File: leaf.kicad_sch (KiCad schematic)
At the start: 0 parts

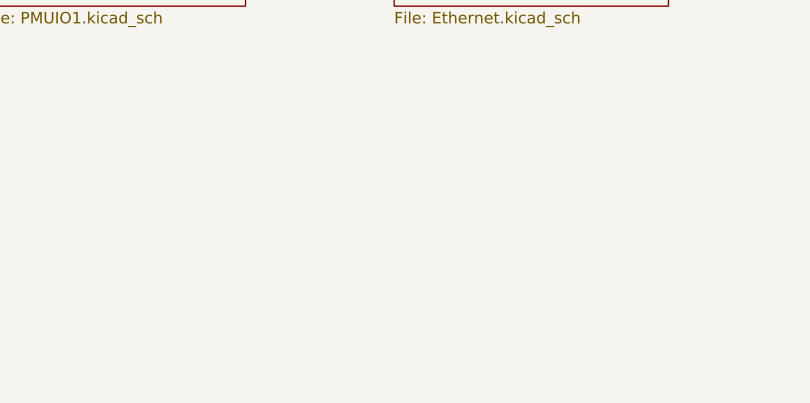
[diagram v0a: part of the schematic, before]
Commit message: placed RK809 components
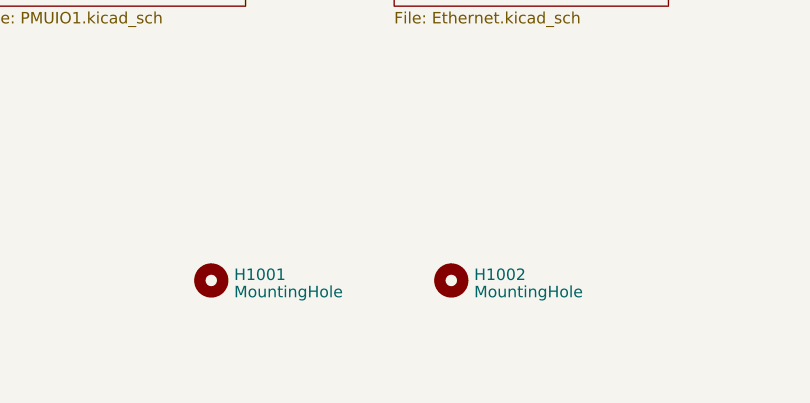
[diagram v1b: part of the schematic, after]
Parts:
- added H1001, H1002: MountingHole, MountingHole:MountingHole_2.7mm_M2.5, symbol Mechanical:MountingHole
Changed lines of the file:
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@@
     (effects (font (size 1.27 1.27)) (justify right bottom))
+  )
+  (symbol (lib_id "Mechanical:MountingHole") (at 106.68 144.78 0) (unit 1)
+    (in_bom yes) (on_board yes) (dnp no) (fields_autoplaced)
+    (property "Reference" "H1001" (at 109.22 144.1363 0)
+      (effects (font (size 1.27 1.27)) (justify left))
+    )
+    (property "Value" "MountingHole" (at 109.22 146.0573 0)
+      (effects (font (size 1.27 1.27)) (justify left))
+    )
+    (property "Footprint" "MountingHole:MountingHole_2.7mm_M2.5" (at 106.68 144.78 0)
+      (effects (font (size 1.27 1.27)) hide)
+    )
+    (property "Datasheet" "~" (at 106.68 144.78 0)
+      (effects (font (size 1.27 1.27)) hide)
+    )
+    (instances
+      (project "leaf"
+        (path "/e3b58043-16a3-43c8-9fad-9c9784eebfa4"
+          (reference "H1001") (unit 1)
+        )
+      )
+    )
+  )
+  (symbol (lib_id "Mechanical:MountingHole") (at 133.35 144.78 0) (unit 1)
+    (in_bom yes) (on_board yes) (dnp no) (fields_autoplaced)
+    (property "Reference" "H1002" (at 135.89 144.1363 0)
+      (effects (font (size 1.27 1.27)) (justify left))
+    )
+    (property "Value" "MountingHole" (at 135.89 146.0573 0)
+      (effects (font (size 1.27 1.27)) (justify left))
+    )
+    (property "Footprint" "MountingHole:MountingHole_2.7mm_M2.5" (at 133.35 144.78 0)
+      (effects (font (size 1.27 1.27)) hide)
+    )
+    (property "Datasheet" "~" (at 133.35 144.78 0)
+      (effects (font (size 1.27 1.27)) hide)
+    )
+    (instances
+      (project "leaf"
+        (path "/e3b58043-16a3-43c8-9fad-9c9784eebfa4"
+          (reference "H1002") (unit 1)
+        )
+      )
+    )
   )
   (sheet (at 81.28 69.85) (size 29.21 17.78) (fields_autoplaced)

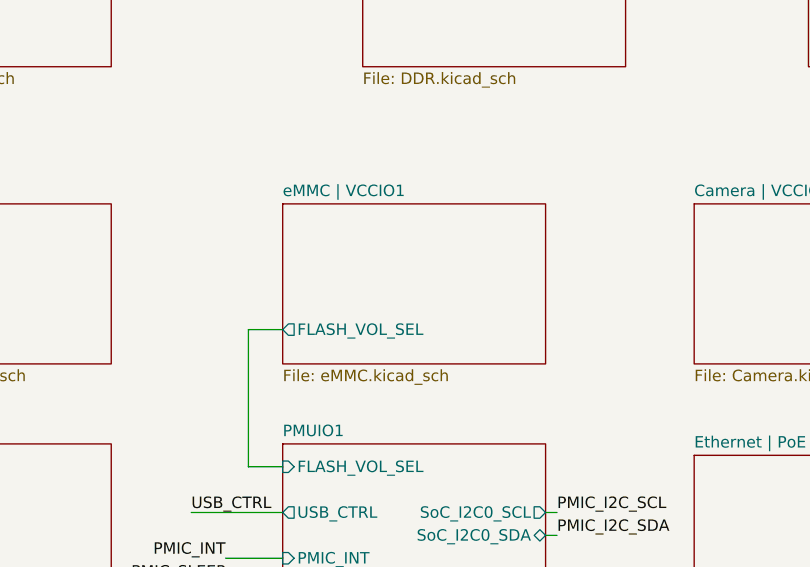
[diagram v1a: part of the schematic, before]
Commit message: rename emmc to vccio1
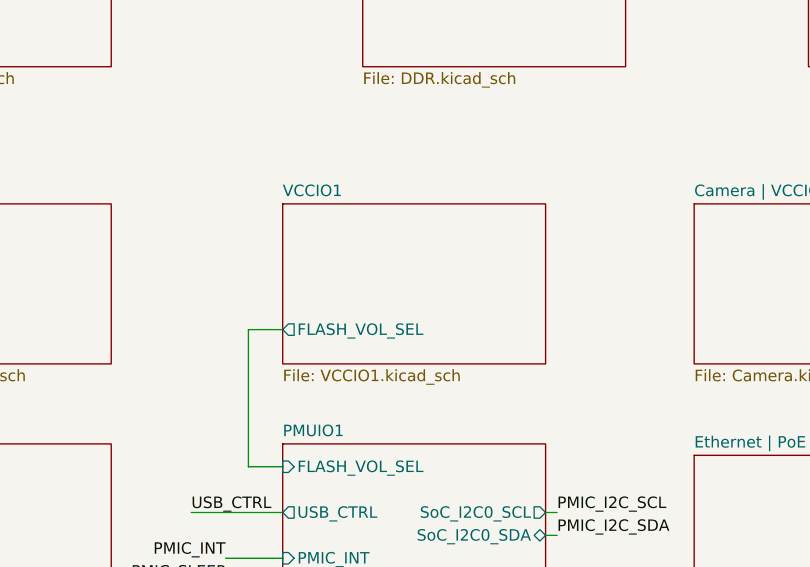
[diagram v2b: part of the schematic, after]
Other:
- sheet eMMC | VCCIO1 renamed VCCIO1
- sheet VCCIO1: file eMMC.kicad_sch -> VCCIO1.kicad_sch
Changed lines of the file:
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@@
     (stroke (width 0.1524) (type solid))
     (fill (color 0 0 0 0.0000))
-    (property "Sheetname" "eMMC | VCCIO1" (at 81.28 69.1384 0)
+    (property "Sheetname" "VCCIO1" (at 81.28 69.1384 0)
       (effects (font (size 1.27 1.27)) (justify left bottom))
     )
-    (property "Sheetfile" "eMMC.kicad_sch" (at 81.28 88.2146 0)
+    (property "Sheetfile" "VCCIO1.kicad_sch" (at 81.28 88.2146 0)
       (effects (font (size 1.27 1.27)) (justify left top))
     )

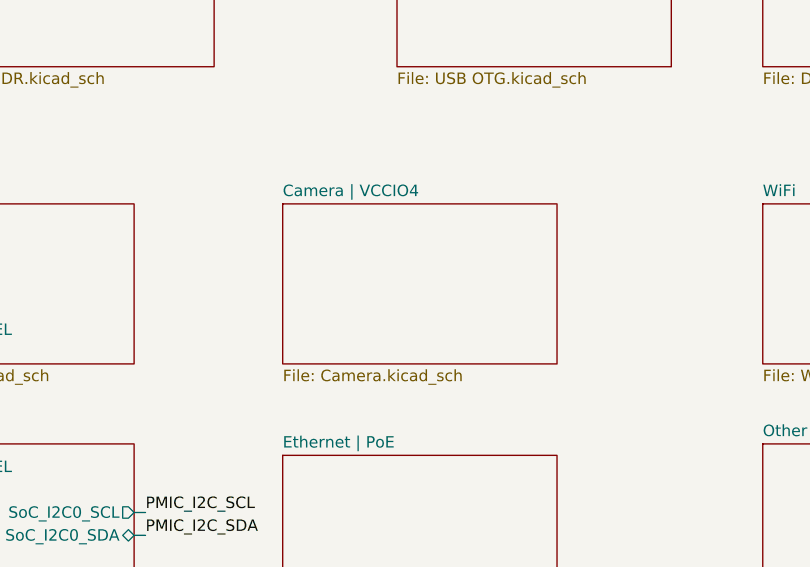
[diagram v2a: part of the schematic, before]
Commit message: rename Camera to VCCIO4
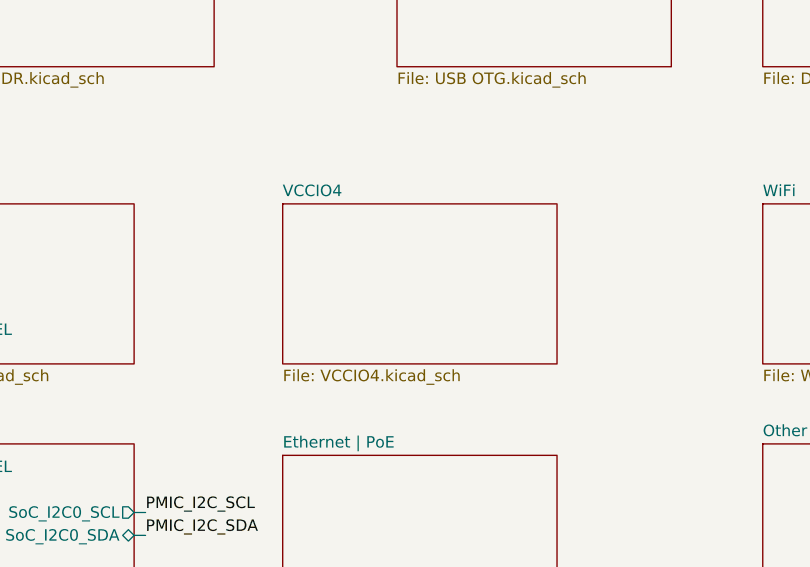
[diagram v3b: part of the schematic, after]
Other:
- sheet Camera | VCCIO4 renamed VCCIO4
- sheet VCCIO4: file Camera.kicad_sch -> VCCIO4.kicad_sch
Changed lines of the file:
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@@
     (stroke (width 0.1524) (type solid))
     (fill (color 0 0 0 0.0000))
-    (property "Sheetname" "Camera | VCCIO4" (at 127 69.1384 0)
+    (property "Sheetname" "VCCIO4" (at 127 69.1384 0)
       (effects (font (size 1.27 1.27)) (justify left bottom))
     )
-    (property "Sheetfile" "Camera.kicad_sch" (at 127 88.2146 0)
+    (property "Sheetfile" "VCCIO4.kicad_sch" (at 127 88.2146 0)
       (effects (font (size 1.27 1.27)) (justify left top))
     )

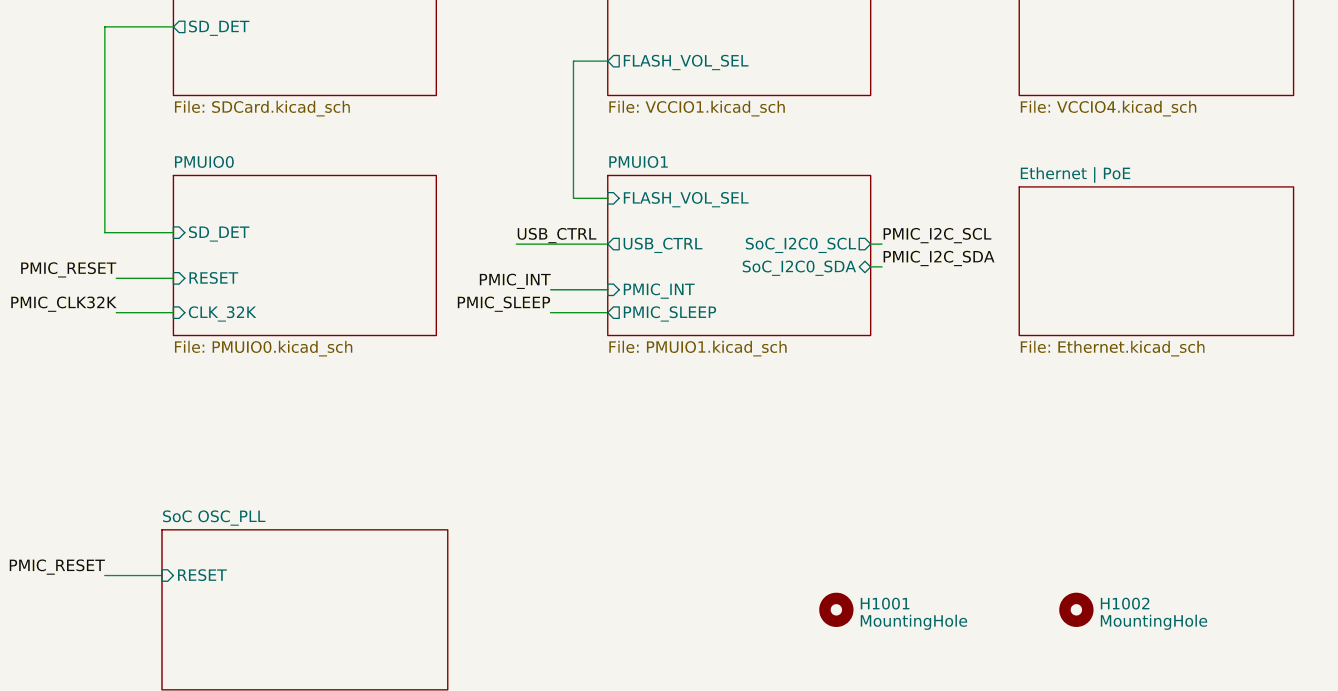
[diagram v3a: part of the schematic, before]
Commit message: rename sub sheets name
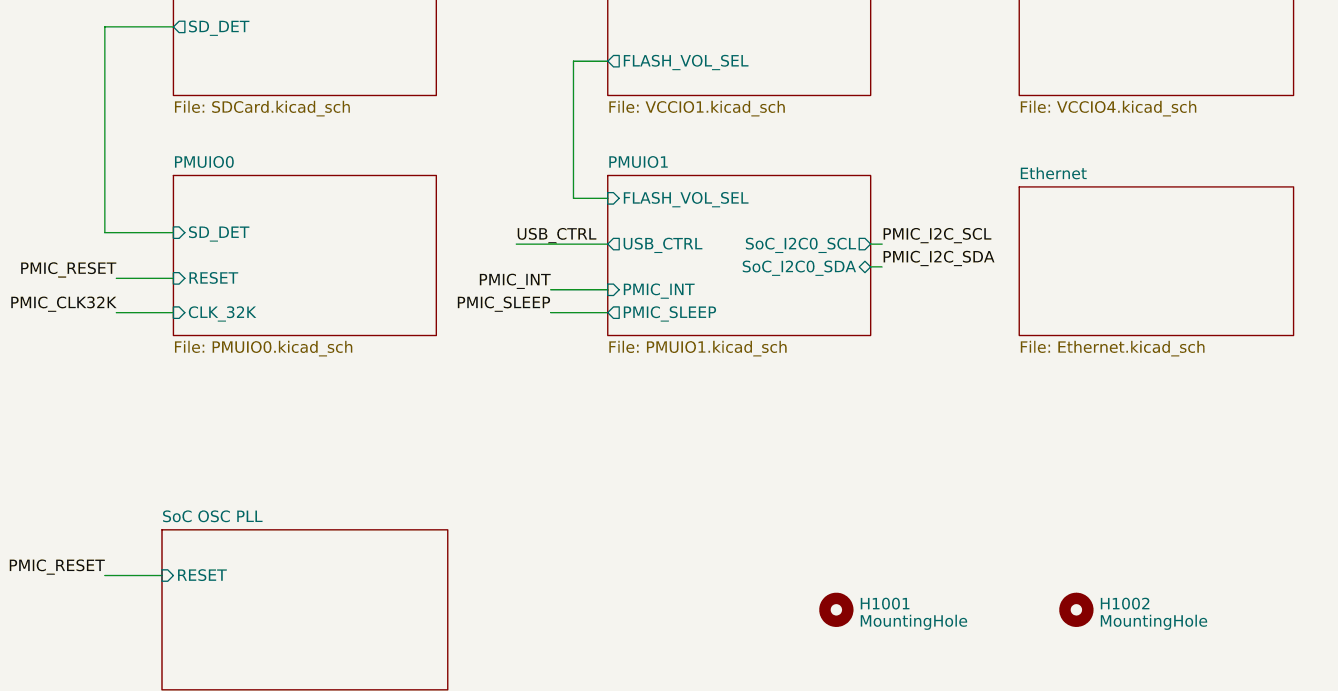
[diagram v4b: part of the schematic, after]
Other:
- sheet Ethernet | PoE renamed Ethernet
- sheet SoC OSC_PLL renamed SoC OSC PLL
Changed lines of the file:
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@@
     (stroke (width 0.1524) (type solid))
     (fill (color 0 0 0 0.0000))
-    (property "Sheetname" "SoC OSC_PLL" (at 31.75 135.1784 0)
+    (property "Sheetname" "SoC OSC PLL" (at 31.75 135.1784 0)
       (effects (font (size 1.27 1.27)) (justify left bottom))
     )
@@
     (stroke (width 0.1524) (type solid))
     (fill (color 0 0 0 0.0000))
-    (property "Sheetname" "Ethernet | PoE" (at 127 97.0784 0)
+    (property "Sheetname" "Ethernet" (at 127 97.0784 0)
       (effects (font (size 1.27 1.27)) (justify left bottom))
     )

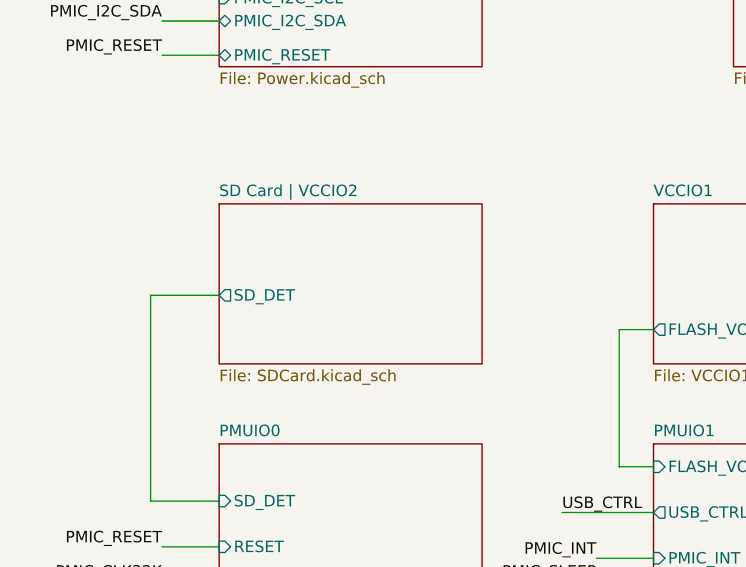
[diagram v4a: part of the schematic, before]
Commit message: rename SDCard to VCCIO2
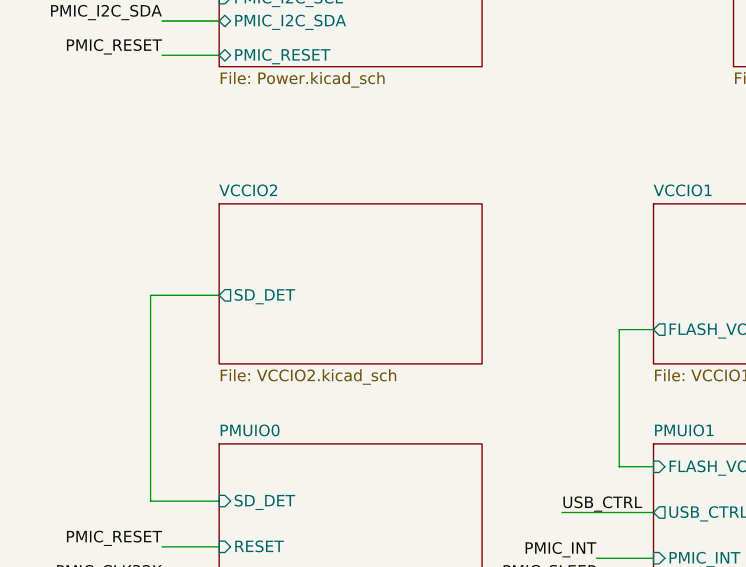
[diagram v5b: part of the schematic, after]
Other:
- sheet SD Card | VCCIO2 renamed VCCIO2
- sheet VCCIO2: file SDCard.kicad_sch -> VCCIO2.kicad_sch
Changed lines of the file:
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@@
     (stroke (width 0.1524) (type solid))
     (fill (color 0 0 0 0.0000))
-    (property "Sheetname" "SD Card | VCCIO2" (at 33.02 69.1384 0)
+    (property "Sheetname" "VCCIO2" (at 33.02 69.1384 0)
       (effects (font (size 1.27 1.27)) (justify left bottom))
     )
-    (property "Sheetfile" "SDCard.kicad_sch" (at 33.02 88.2146 0)
+    (property "Sheetfile" "VCCIO2.kicad_sch" (at 33.02 88.2146 0)
       (effects (font (size 1.27 1.27)) (justify left top))
     )

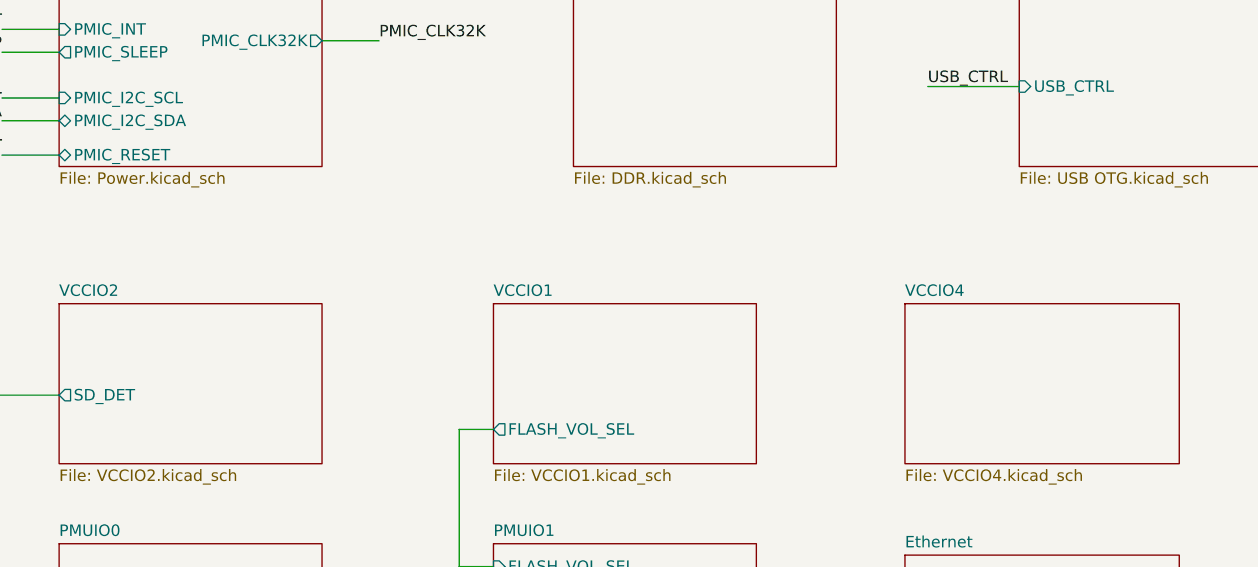
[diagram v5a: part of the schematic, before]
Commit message: added text label for renamed hierarchical sheets
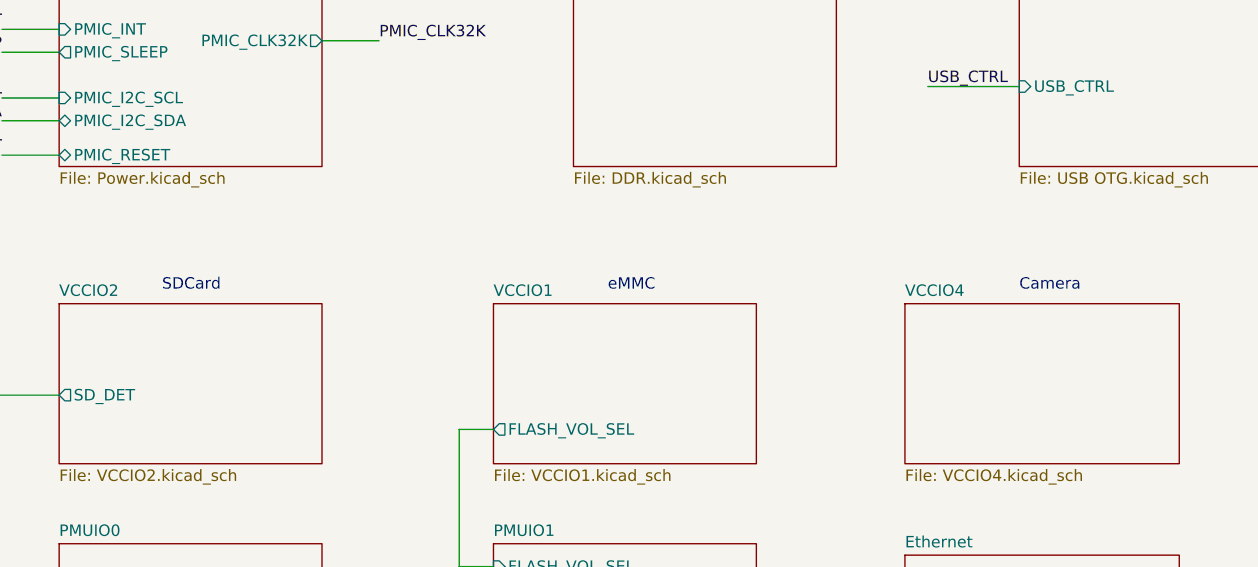
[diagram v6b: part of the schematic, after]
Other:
- note added: "Camera"
- note added: "SDCard"
- note added: "eMMC"
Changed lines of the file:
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@@
     (stroke (width 0) (type default))
+  )
+  (text "Camera" (at 139.7 68.58 0)
+    (effects (font (size 1.27 1.27)) (justify left bottom))
+  )
+  (text "SDCard" (at 44.45 68.58 0)
+    (effects (font (size 1.27 1.27)) (justify left bottom))
+  )
+  (text "eMMC" (at 93.98 68.58 0)
+    (effects (font (size 1.27 1.27)) (justify left bottom))
   )
   (label "PMIC_SLEEP" (at 74.93 111.76 180) (fields_autoplaced)

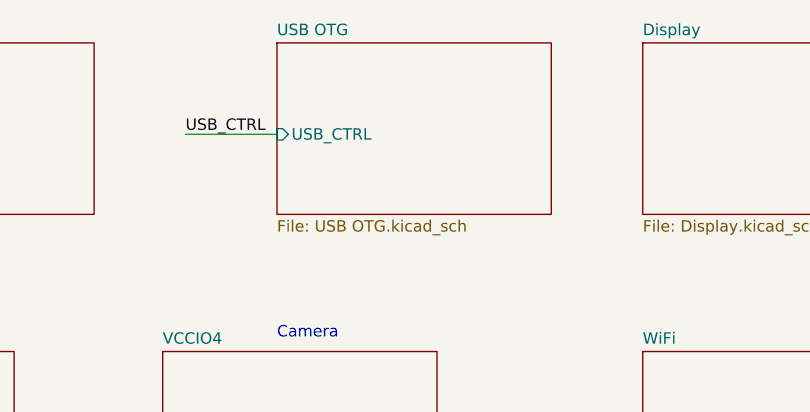
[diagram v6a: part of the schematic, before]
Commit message: rename USB OTG to USB
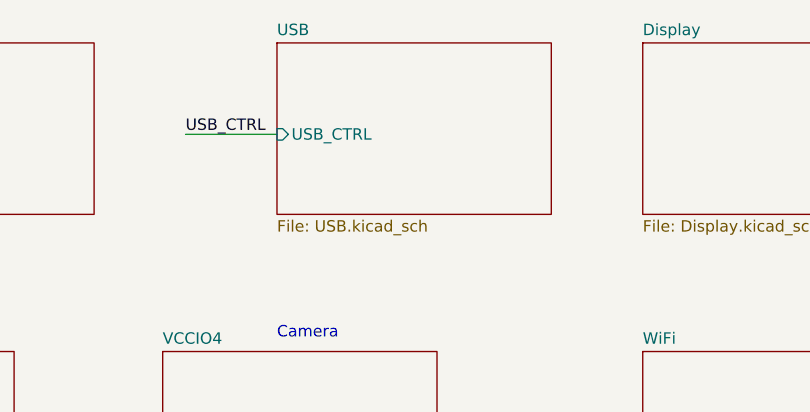
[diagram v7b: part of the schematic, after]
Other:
- sheet USB OTG renamed USB
- sheet USB: file USB OTG.kicad_sch -> USB.kicad_sch
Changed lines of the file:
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@@
     (stroke (width 0.1524) (type solid))
     (fill (color 0 0 0 0.0000))
-    (property "Sheetname" "USB OTG" (at 139.7 34.8484 0)
+    (property "Sheetname" "USB" (at 139.7 34.8484 0)
       (effects (font (size 1.27 1.27)) (justify left bottom))
     )
-    (property "Sheetfile" "USB OTG.kicad_sch" (at 139.7 55.1946 0)
+    (property "Sheetfile" "USB.kicad_sch" (at 139.7 55.1946 0)
       (effects (font (size 1.27 1.27)) (justify left top))
     )
